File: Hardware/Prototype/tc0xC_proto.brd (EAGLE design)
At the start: 101.6 x 98.8 mm, 100 parts, among them IC1 AP2112M-3.3TRG1, Q1 2.5A/30V, Q2 MBT3904DW1T1, Q3 600mA/40V, Q4 MBT3904DW1T1, U2 ESP3212, U4 FT231XS, U5 W25Q32FVSS, Y1 26MHz, Y2 32.768kHz

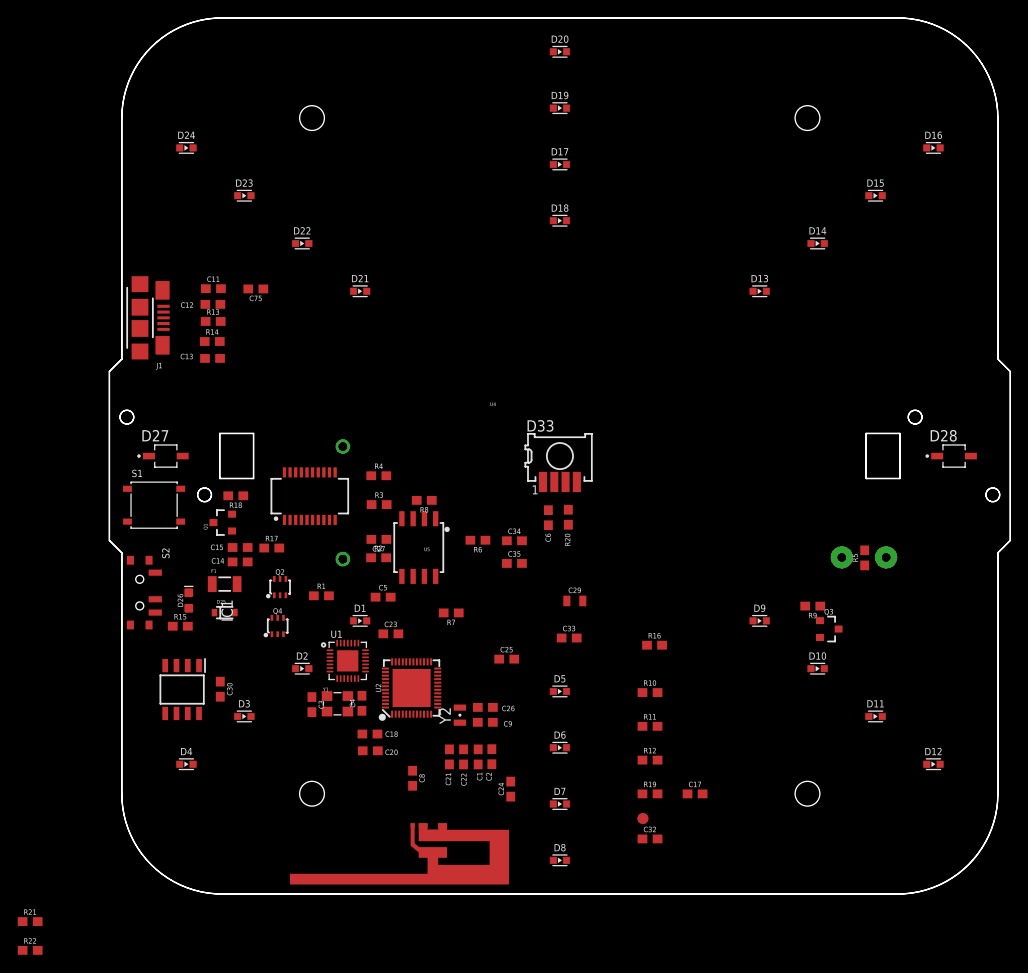
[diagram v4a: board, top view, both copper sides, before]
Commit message: right angle momentary placement
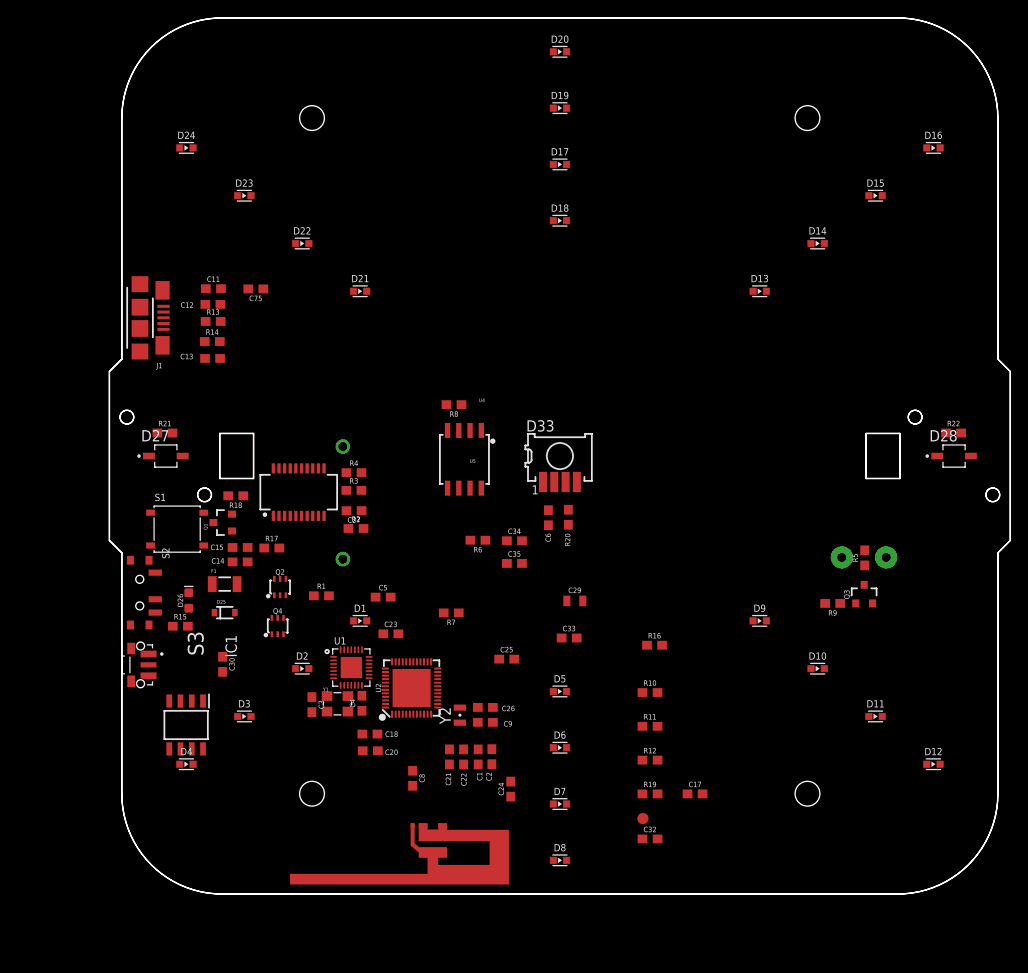
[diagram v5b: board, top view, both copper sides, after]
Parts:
- added S3: TL3340AF160QG, TL3340AF160QG:SW_TL3340AF160QG
- moved R22 119.4 mm to (95.2, 53.4)
- moved R21 57.2 mm to (6.25, 53.4)
- moved R8 11.3 mm to (38.9, 56.6)
- moved U5 11.2 mm to (40.0, 50.4)
- moved Q3 5.57 mm to (85.1, 35.2), turned to 0 degrees
- moved C27 4.29 mm to (27.6, 44.6)
- moved R2 4.17 mm to (27.8, 42.6)
- moved IC1 4.03 mm to (8.64, 20.5)
- moved S1 3.75 mm to (7.63, 42.6)
- moved R3 3.27 mm to (27.6, 46.9)
- moved R4 2.82 mm to (27.6, 48.9)
- moved C30 2.81 mm to (12.8, 27.3)
- moved R9 2.27 mm to (81.6, 34.2)
- moved U4 1.33 mm to (21.3, 46.7)
- moved U1 0.85 mm to (27.3, 26.9)

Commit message: double push rip up
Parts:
- moved IC1 60.2 mm to (29.8, 76.9), turned to 180 degrees
- moved S2 40.3 mm to (3.31, 75.7)
- moved F1 36.3 mm to (11.6, 72.6)
- moved Q1 30.8 mm to (15.8, 73.9), turned to 0 degrees
- moved C33 17.9 mm to (34.3, 33.7)
- moved S3 9.50 mm to (3.60, 36.8)
- moved C4 3.76 mm to (27.0, 19.5)
- moved C18 3.76 mm to (27.9, 16.0)
- moved C20 3.76 mm to (27.9, 14.1)
- moved C3 3.76 mm to (21.3, 19.3)
- moved Y1 3.76 mm to (24.2, 19.4)
- moved U2 1.60 mm to (34.0, 23.0)
- moved U1 0.87 mm to (27.6, 26.1)

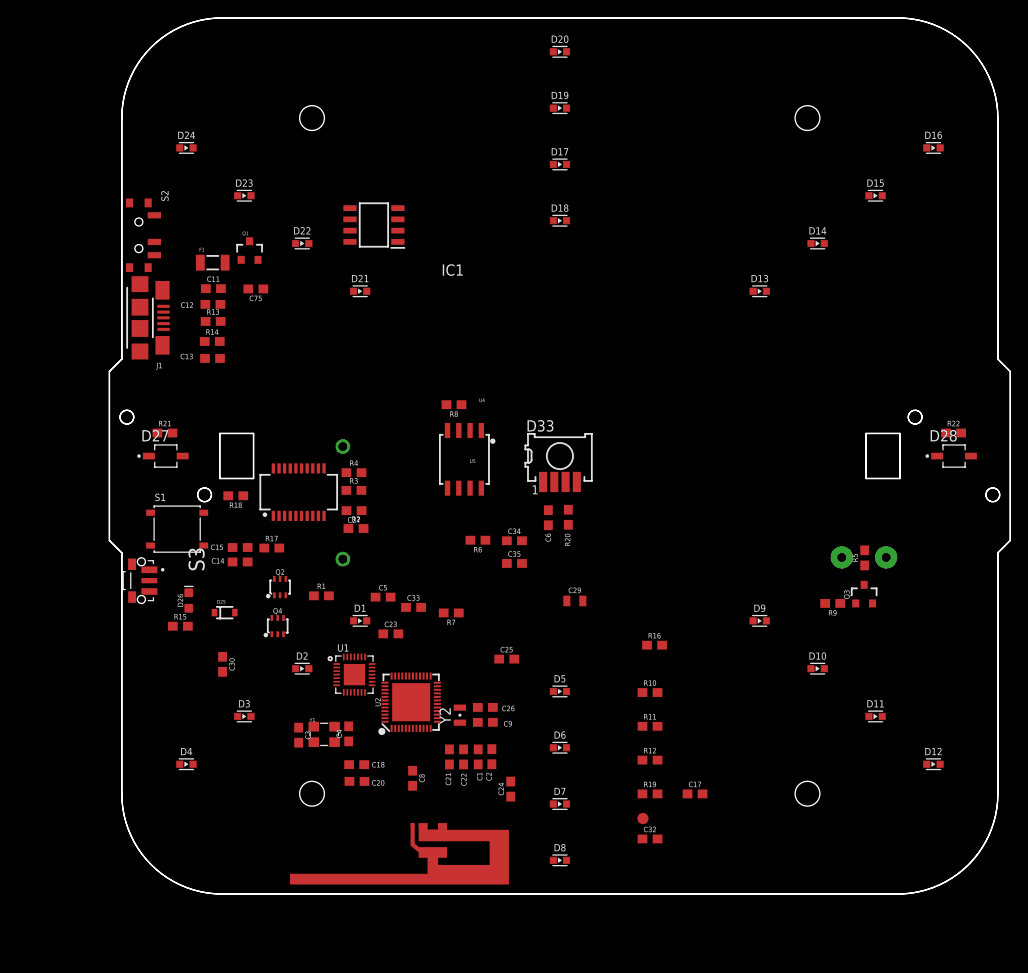
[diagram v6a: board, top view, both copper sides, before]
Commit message: mirror of batt and switch fix complete
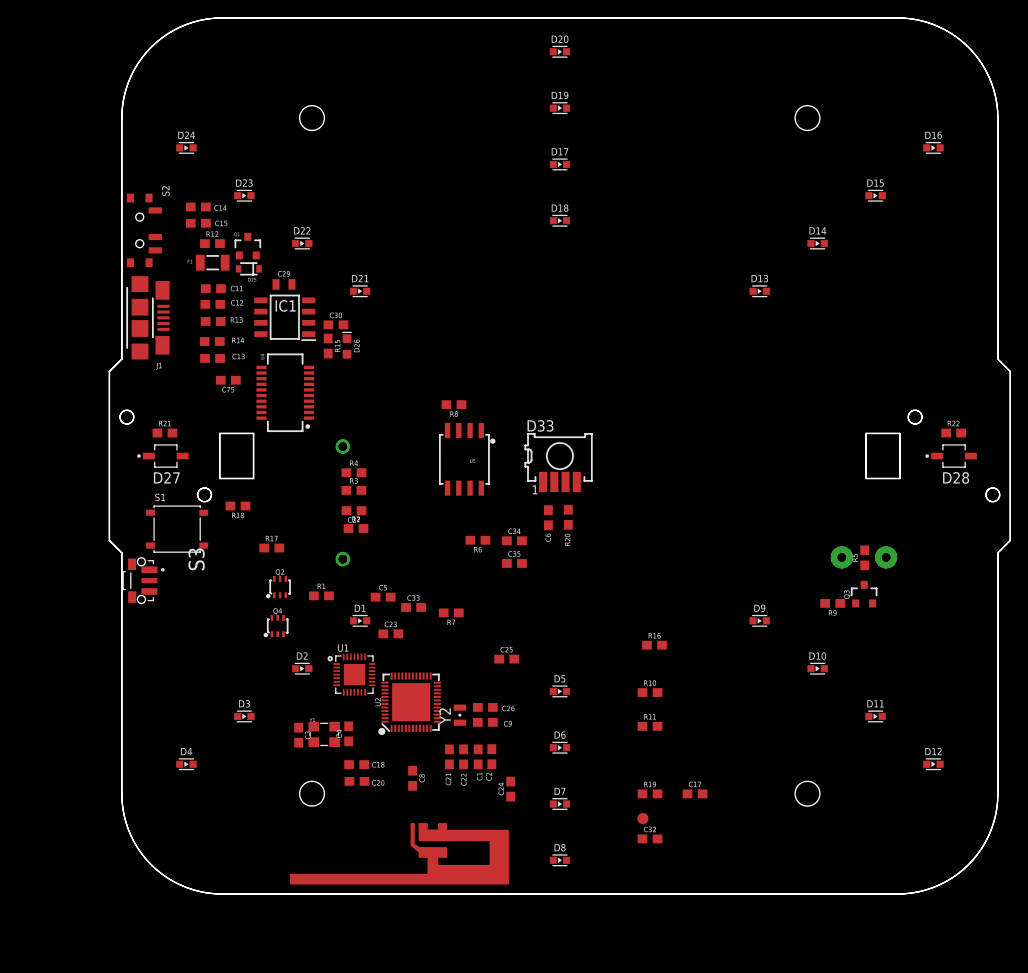
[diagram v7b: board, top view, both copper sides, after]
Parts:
- moved R12 76.3 mm to (11.6, 74.8)
- moved C29 48.5 mm to (19.7, 70.2)
- moved C30 40.4 mm to (25.5, 65.6), turned to 0 degrees
- moved C14 40.3 mm to (10.0, 78.9), turned to 180 degrees
- moved D25 38.9 mm to (15.7, 71.9), turned to 180 degrees
- moved C15 36.9 mm to (10.0, 77.1), turned to 180 degrees
- moved R15 35.7 mm to (24.7, 63.2), turned to 270 degrees
- moved D26 33.8 mm to (26.8, 63.2)
- moved IC1 14.5 mm to (19.8, 66.5)
- moved U4 11.3 mm to (19.8, 57.9), turned to 90 degrees
- moved C75 10.8 mm to (13.4, 59.4)
- moved R18 1.18 mm to (14.5, 45.2)
- moved S2 0.56 mm to (3.41, 76.2)
- moved Q1 0.54 mm to (15.6, 74.4)

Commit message: double push rip up
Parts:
- moved R16 50.0 mm to (11.6, 32.5)
- moved C17 40.3 mm to (44.9, 47.0)
- moved C23 15.6 mm to (46.6, 35.5)
- moved C33 6.65 mm to (39.0, 38.4)
- moved R7 5.28 mm to (33.4, 34.5)
- moved Q2 4.29 mm to (15.0, 36.6)
- moved Q4 3.37 mm to (15.7, 32.3)
- moved C5 2.75 mm to (30.8, 37.6)
- moved U1 0.20 mm to (27.6, 26.4)
